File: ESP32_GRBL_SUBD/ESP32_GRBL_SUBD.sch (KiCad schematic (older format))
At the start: 26 parts, among them J1 DB25_Female_MountingHoles, J2 Micro_SD_Card, J3 Conn_01x19_Female, J3a1 Conn_01x19_Female, J4 Conn_01x19_Female, J4a1 Conn_01x19_Female, J5 Barrel_Jack_MountingPin, J6 Screw_Terminal_01x02, J7 Screw_Terminal_01x02, J8 Screw_Terminal_01x02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

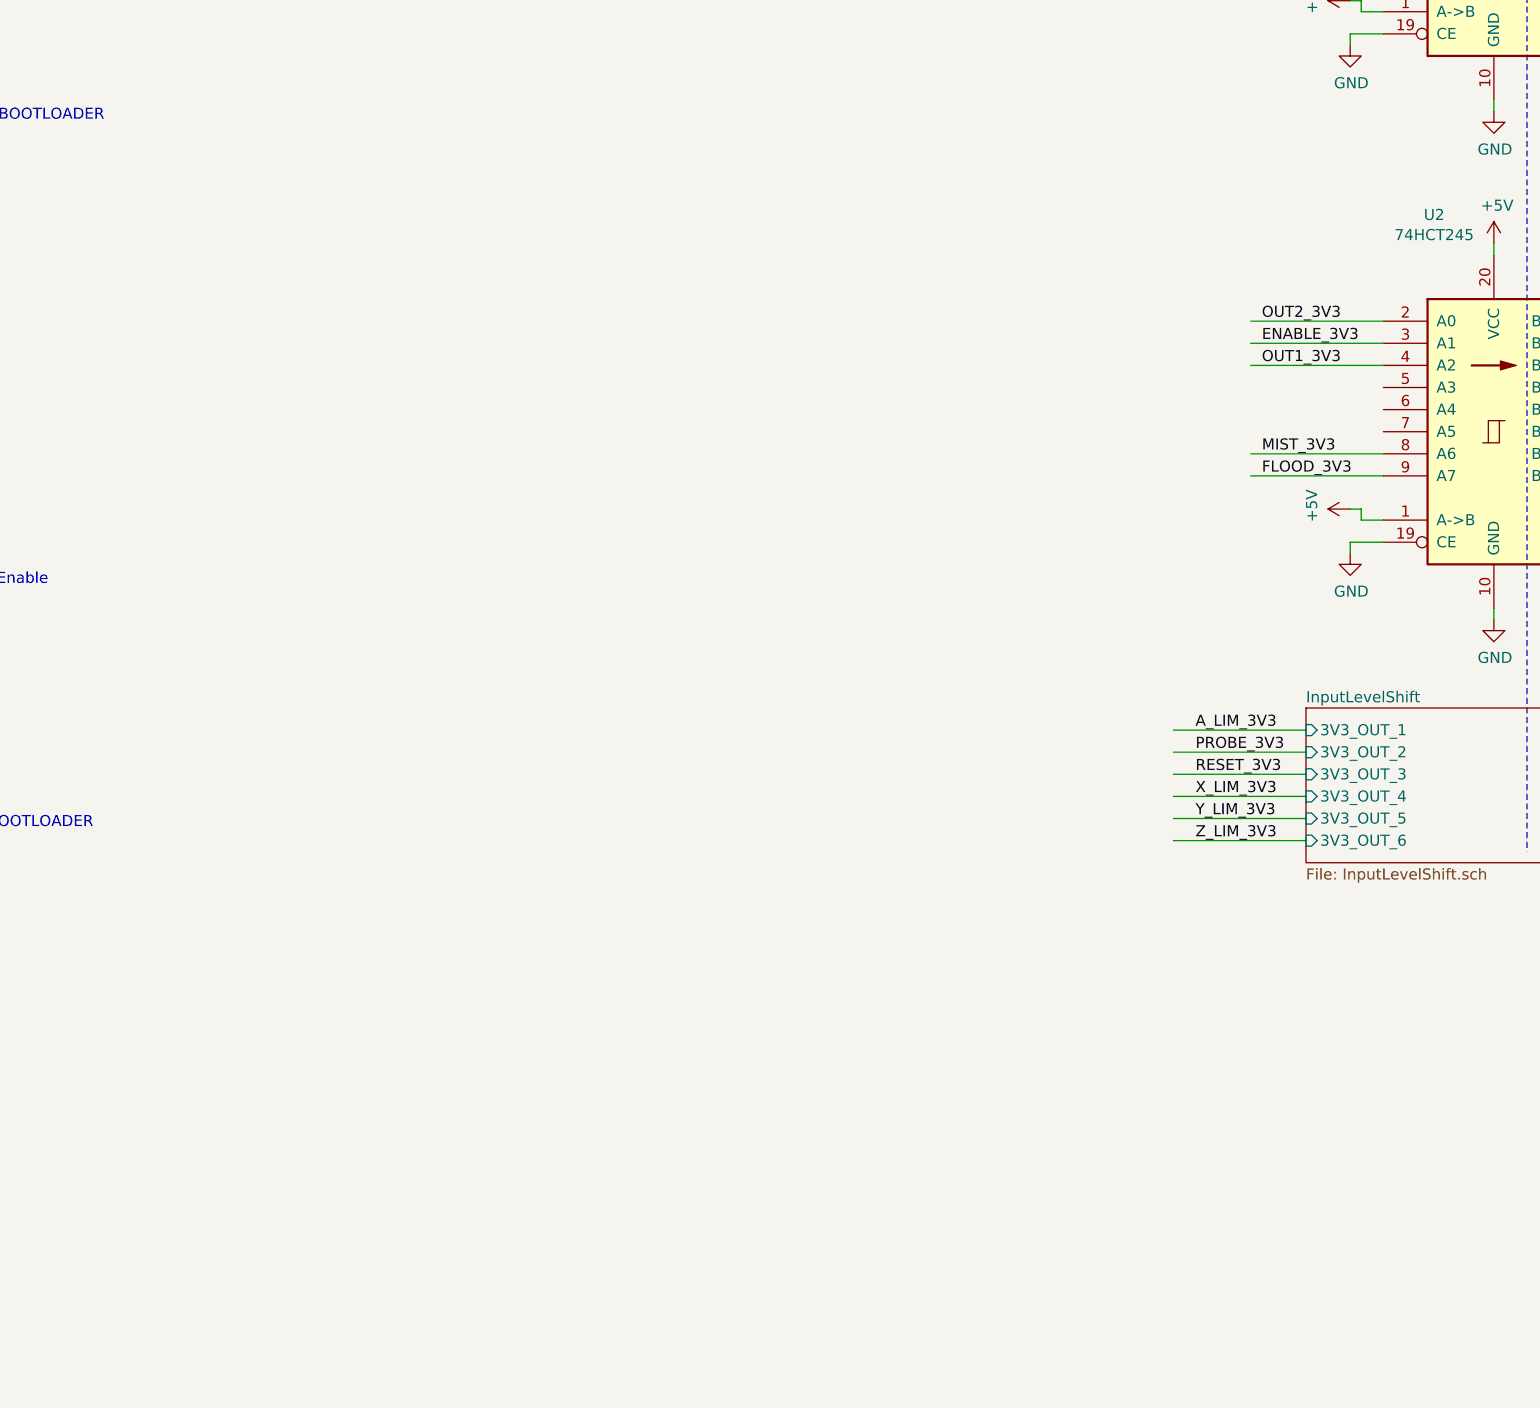
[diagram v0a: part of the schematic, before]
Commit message: added resistors to map outputs to different pins on SUB-D
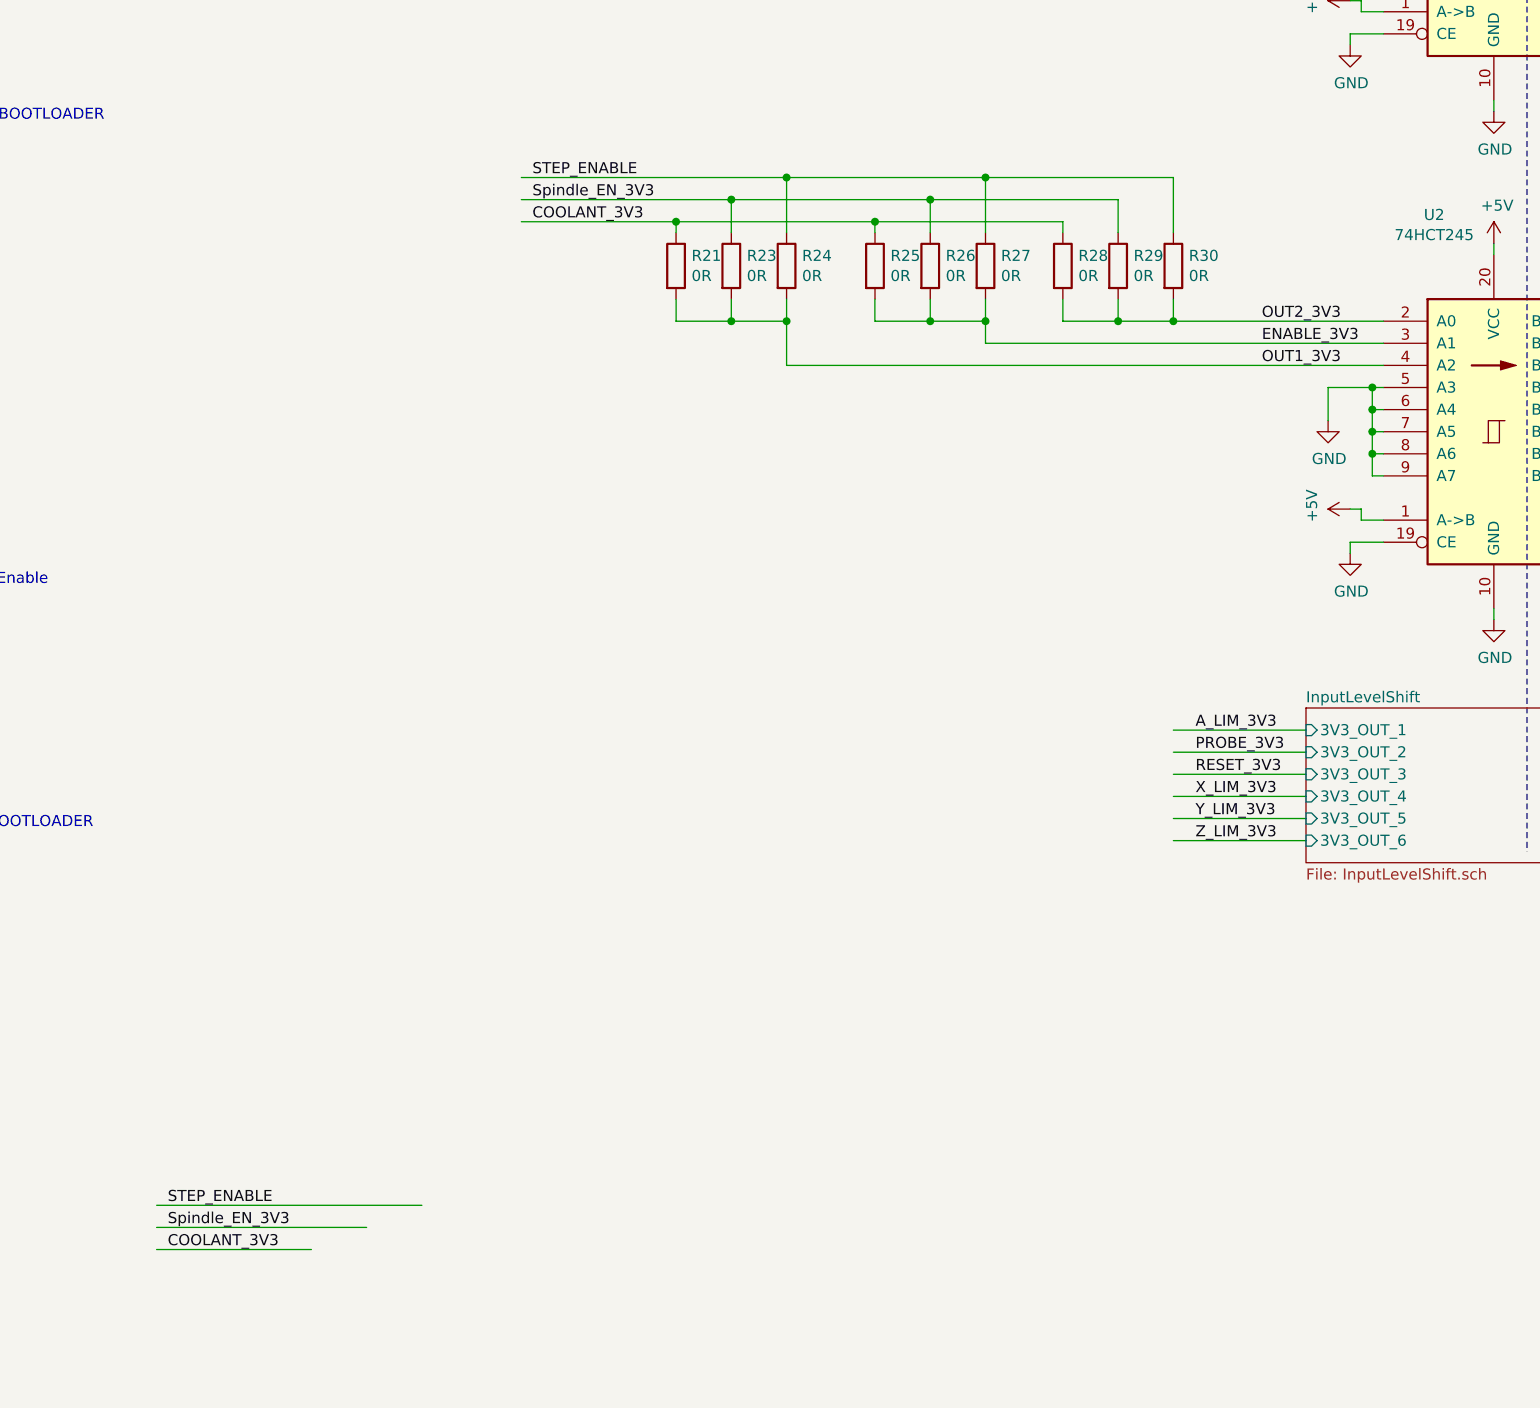
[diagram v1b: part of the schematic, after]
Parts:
- added R21, R23, R24, R25, R26, R27, R28, R29, R30: 0R, Resistor_SMD:R_0603_1608Metric, symbol Device:R
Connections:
- net labels removed: FLOOD_3V3, MIST_3V3
- wire segments 203 -> 250

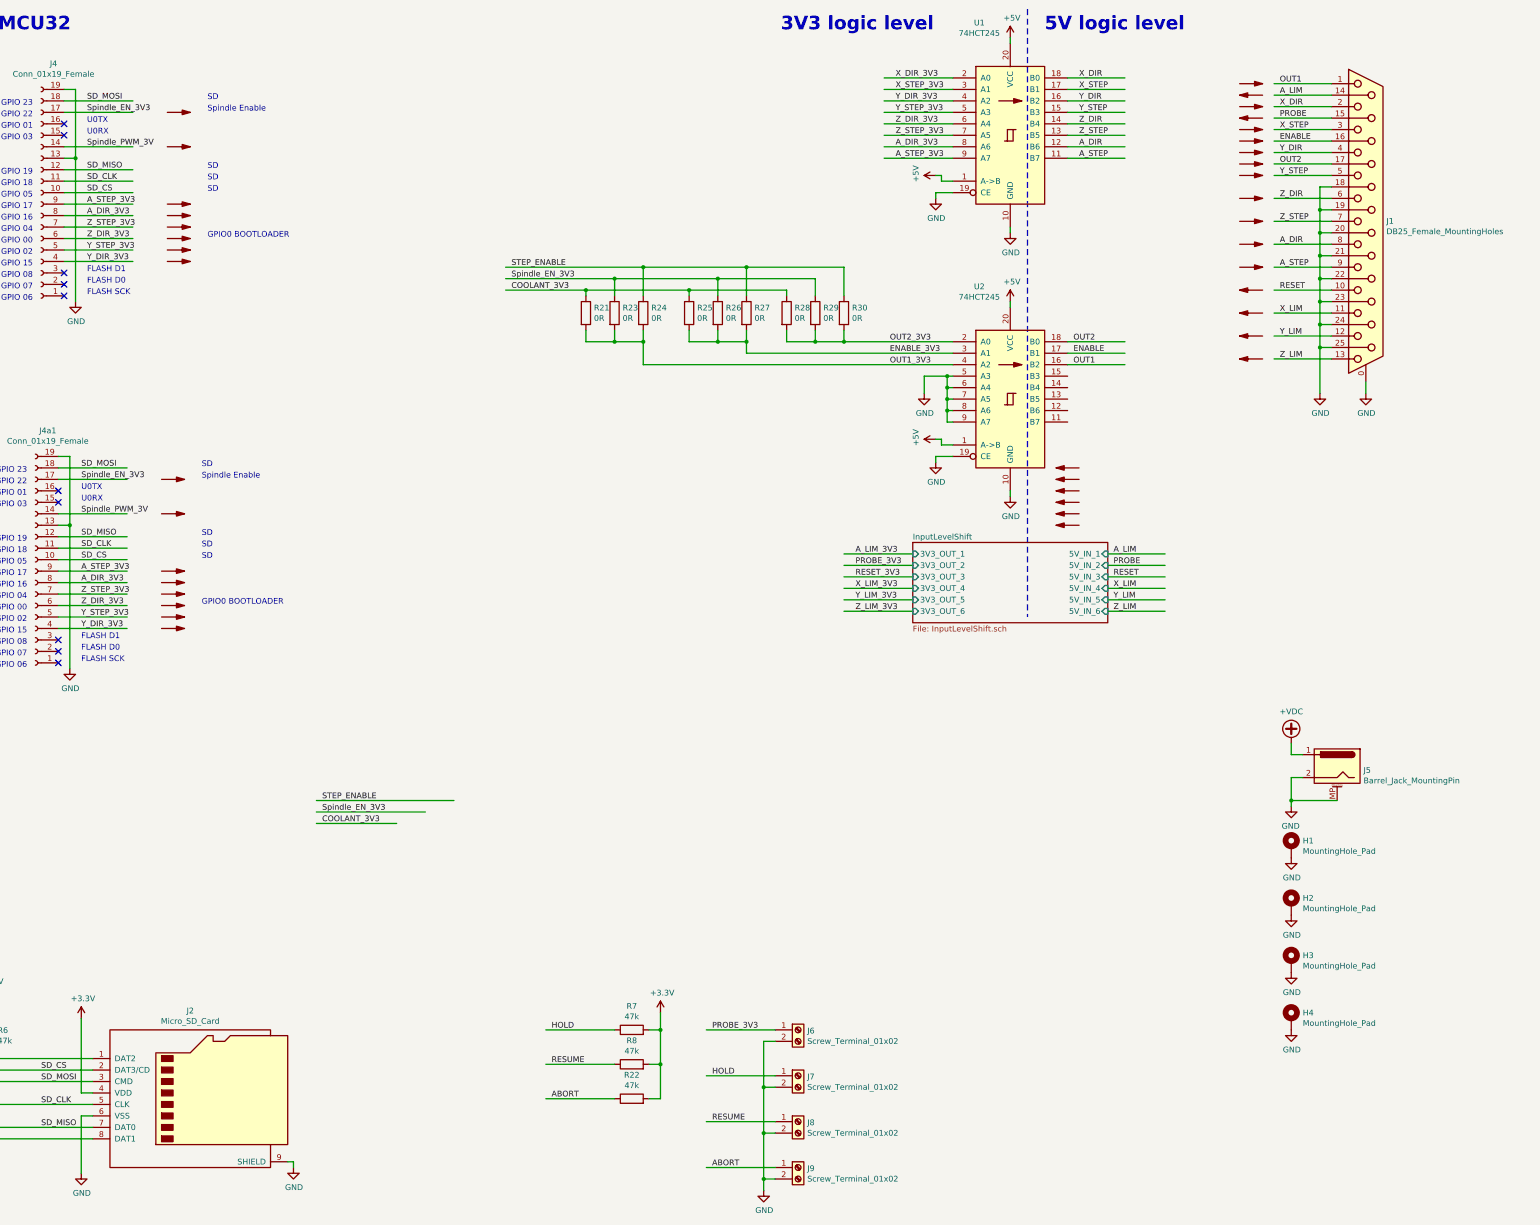
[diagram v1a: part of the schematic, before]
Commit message: added level converter for outputs and some LEDs for limit switches
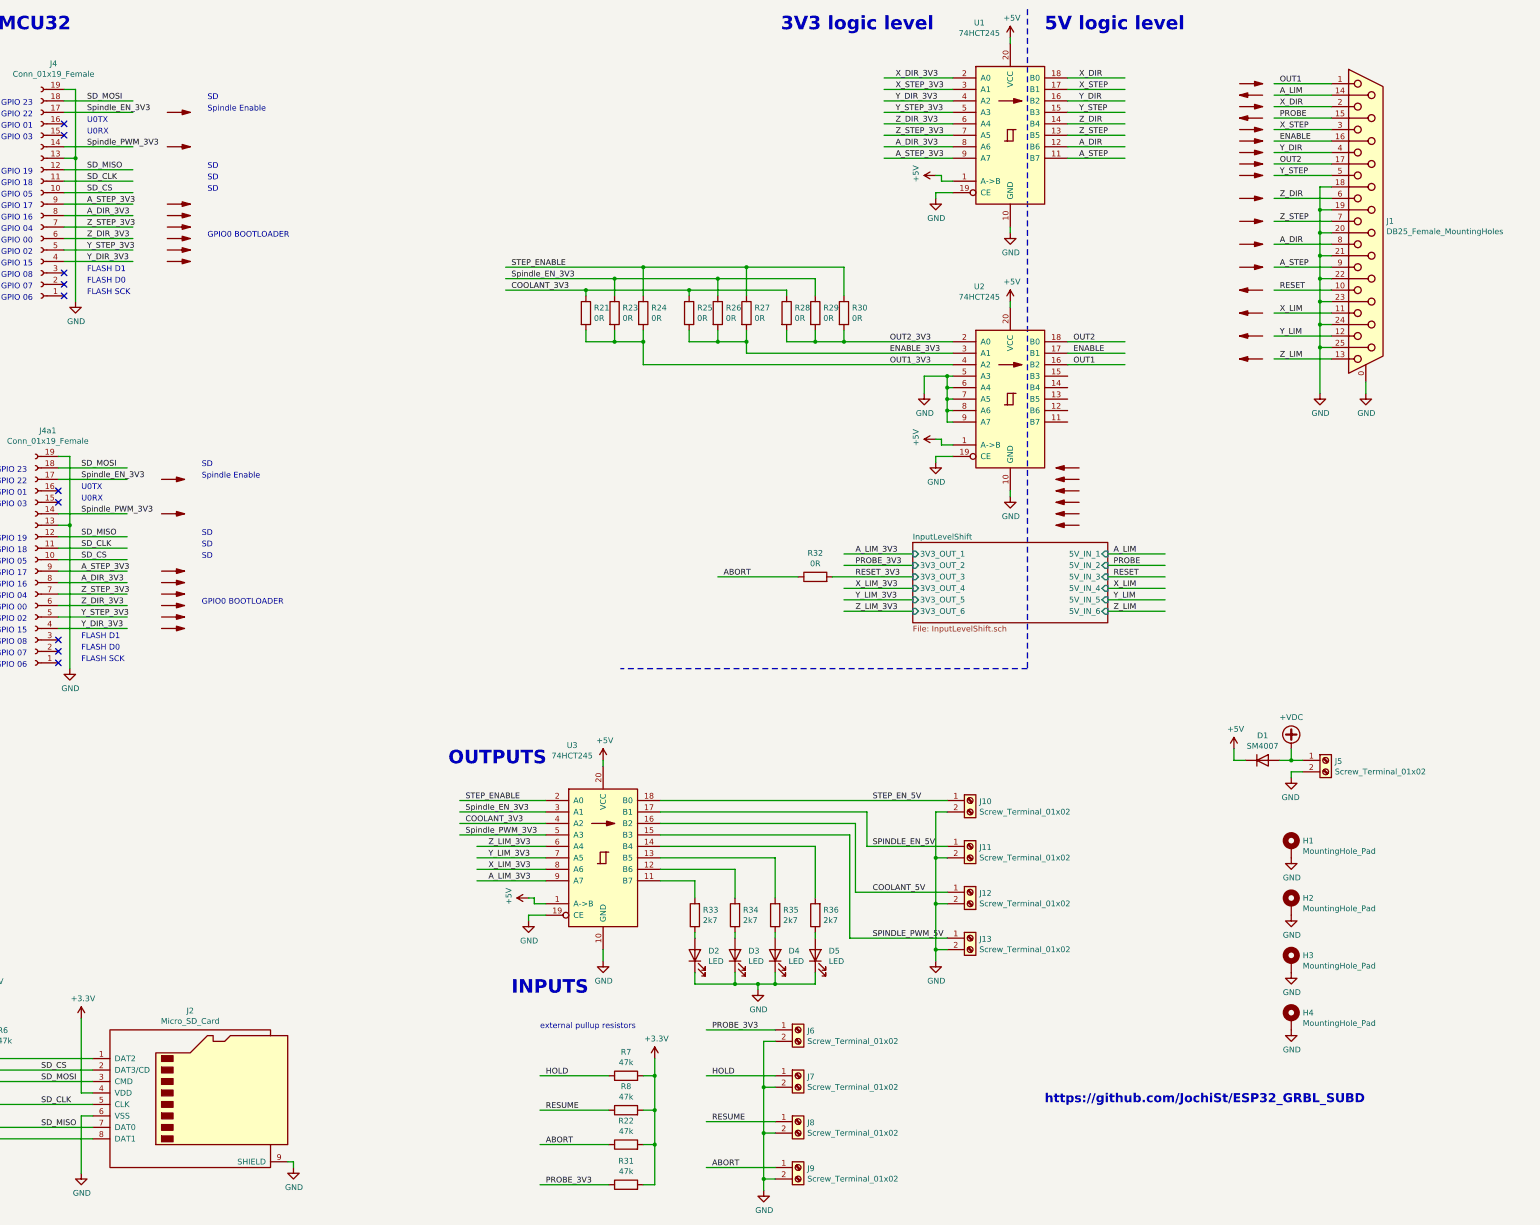
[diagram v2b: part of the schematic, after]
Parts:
- removed J5: Barrel_Jack_MountingPin, Connector_BarrelJack:BarrelJack_CUI_PJ-063AH_Horizontal, symbol Connector:Barrel_Jack_MountingPin
- added D1: SM4007, Diode_SMD:D_MELF, symbol Diode:SM4007
- added D2, D3, D4, D5: LED, LED_SMD:LED_0603_1608Metric, symbol Device:LED
- added J10, J11, J12, J13, J5: Screw_Terminal_01x02, TerminalBlock_MetzConnect:TerminalBlock_MetzConnect_Type055_RT01502HDWU_1x02_P5.00mm_Horizontal, symbol Connector:Screw_Terminal_01x02
- added R31: 47k, Resistor_SMD:R_0603_1608Metric, symbol Device:R
- added R32: 0R, Resistor_SMD:R_0603_1608Metric, symbol Device:R
- added R33, R34, R35, R36: 2k7, Resistor_SMD:R_0603_1608Metric, symbol Device:R
- added U3: 74HCT245, Package_SO:SO-20_12.8x7.5mm_P1.27mm, symbol 74xx:74HC245
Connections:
- net labels added: COOLANT_5V, SPINDLE_EN_5V, SPINDLE_PWM_5V, STEP_EN_5V, Spindle_PWM_3V3
- net labels removed: Spindle_PWM_3V
- wire segments 250 -> 306
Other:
- note added: "INPUTS"
- note added: "OUTPUTS"
- note added: "external pullup resistors"
- note added: "https://github.com/JochiSt/ESP32_GRBL_SUBD"
- moved on the sheet: R22, R7, R8
